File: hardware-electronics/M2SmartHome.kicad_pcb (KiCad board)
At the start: 4 copper layers, 22 x 76 mm, 207 parts, among them J1 M.2-Key-M-edge-connector, J2 Micro_SD_Card_Det_Hirose_DM3AT, J3 CONMHF1-SMD-T, J4 CONMHF1-SMD-T, U1 RTL8188FTV-VC-CG, U10 24AA04T-I_OT, U2 EMMC16G-MW28-01E10, U3 PI7C9X440SLBFDE, U4 24AA04T-I_OT, U5 CP2102N-A02-GQFN20, U6 24AA04T-I_OT, U7 EFR32MG21B020F1024IM32-B, U8 USB2244-AEZG-06, U9 USB2244-AEZG-06, Y1 ABM8-12.000MHZ-B2-T, Y2 ECS-240-10-47-CKM-TR, Y3 ECS-240-10-47-CKM-TR, Y5 ABM8-40.000MHZ-B2-T

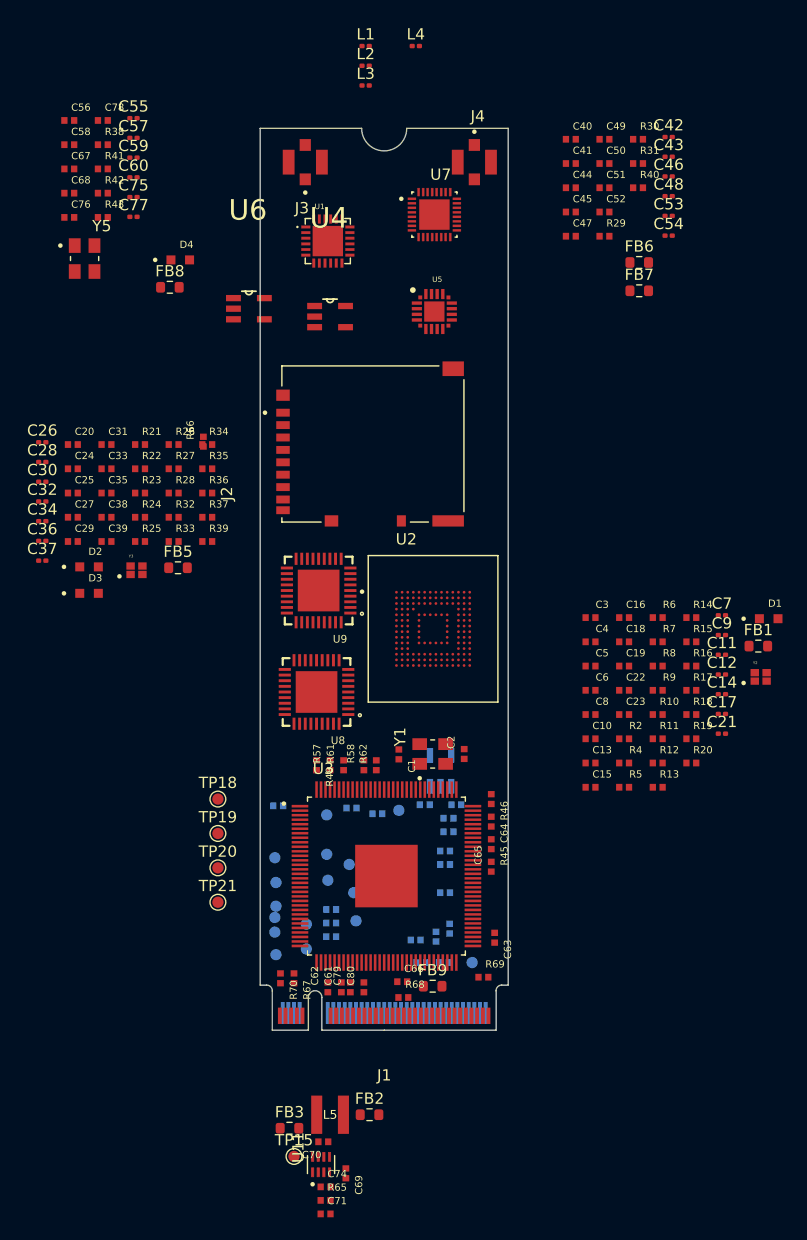
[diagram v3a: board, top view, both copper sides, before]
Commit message: [#13] WIP Placement wifi
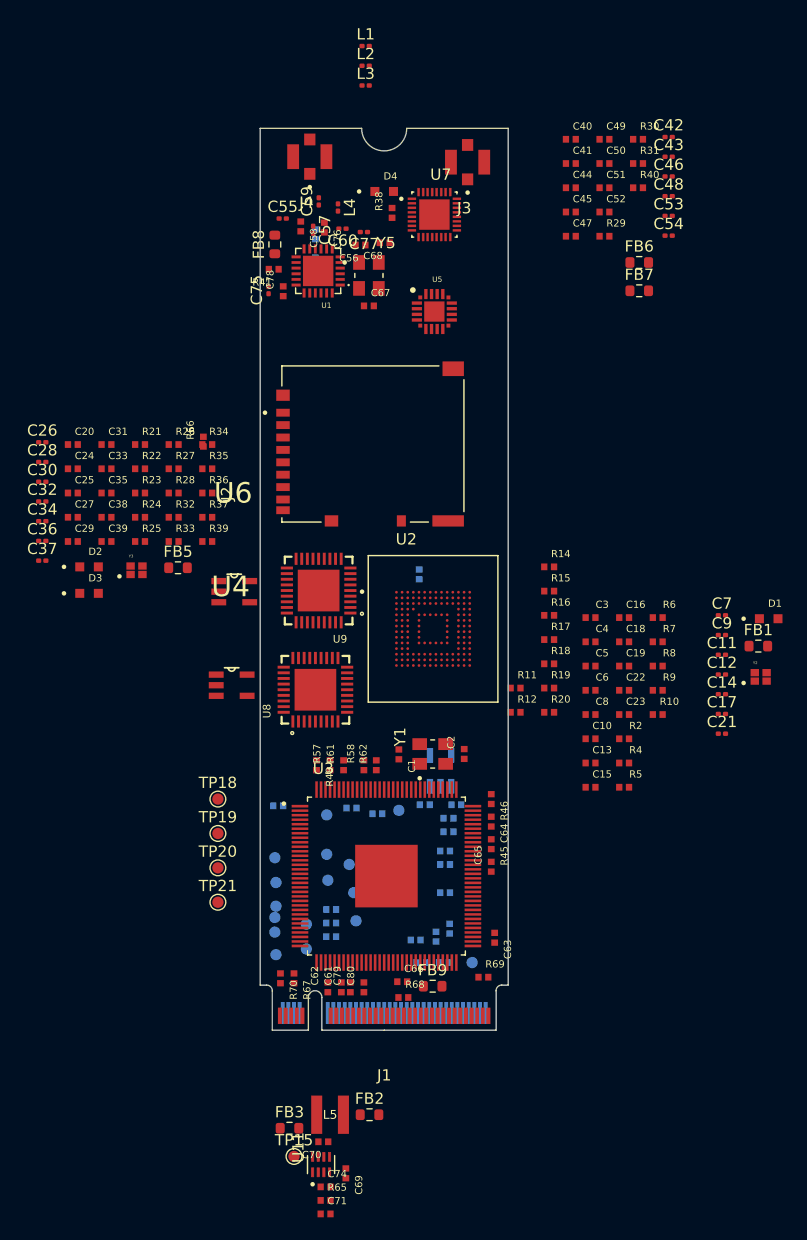
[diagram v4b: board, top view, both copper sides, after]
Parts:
- R13, R42, R43: moved to B.Cu
- moved U4 33.8 mm to (78.5, 135.4)
- moved C67 29.2 mm to (90.6, 101.8)
- moved R13 28.4 mm to (95.1, 125.6), turned to 90 degrees
- moved C68 28.3 mm to (92.0, 96.2), turned to 180 degrees
- moved C56 28.1 mm to (89.9, 96.3), turned to 180 degrees
- moved R38 26.4 mm to (92.7, 93.5), turned to 90 degrees
- moved Y5 25.3 mm to (90.6, 99.0)
- moved U6 25.1 mm to (78.7, 127.1)
- moved C76 22.7 mm to (86.7, 94.8), turned to -90 degrees
- moved C78 22.0 mm to (83.0, 100.5), turned to 90 degrees
- moved C58 21.8 mm to (84.6, 94.7), turned to -90 degrees
- moved C77 20.5 mm to (90.2, 95.2), turned to 180 degrees
- moved R43 19.3 mm to (85.9, 97.9), turned to 90 degrees
- moved R42 19.2 mm to (85.9, 95.4), turned to 90 degrees
- moved C60 19.1 mm to (88.3, 94.9), turned to 180 degrees
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
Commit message: [#13] WIP Placement wifi
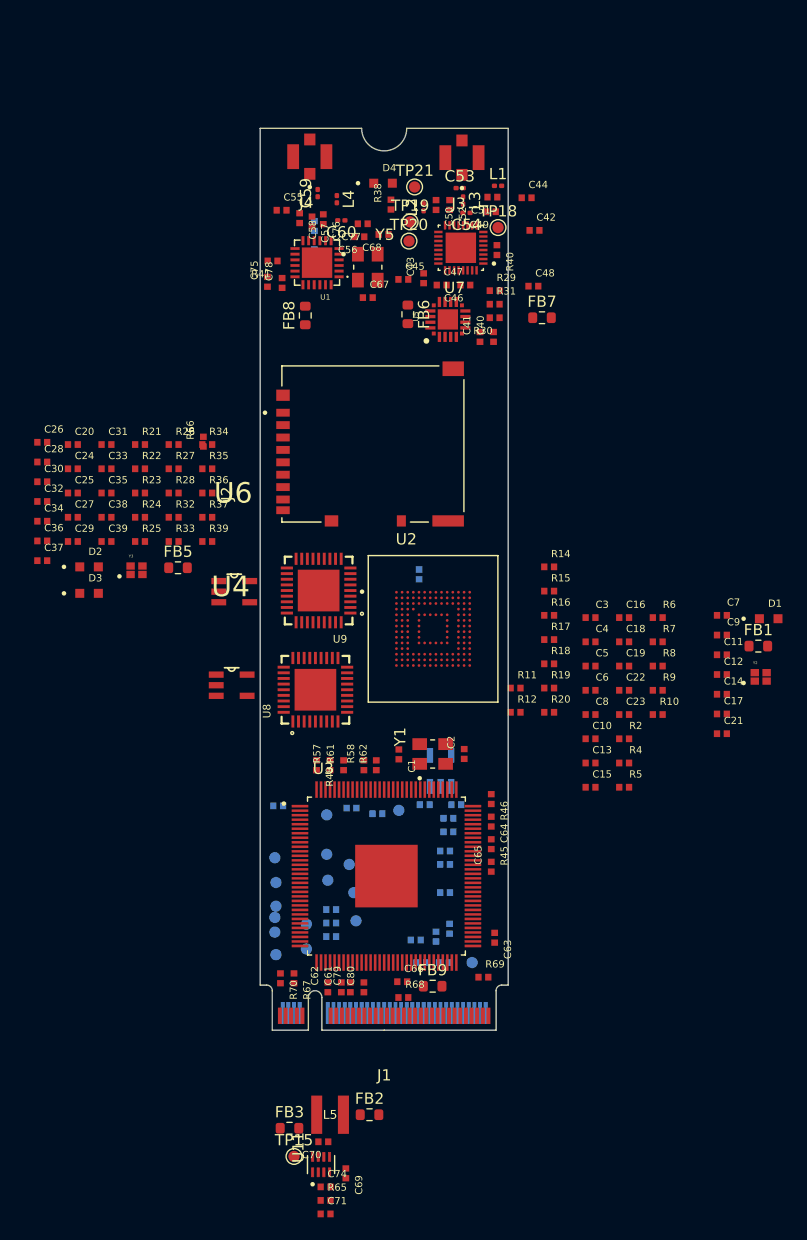
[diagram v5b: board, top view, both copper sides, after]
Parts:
- C11, C12, C14, C17, C21, C26, C28, C30, C32, C34, C36, C37, C42, C43, C46, C48, C55, C57, C7, C75, C77, C9: footprint M2SmartHomeFootprints:C_0201 -> M2SmartHomeFootprints:C_0402
- moved TP21 65.8 mm to (94.7, 91.2)
- moved TP20 58.1 mm to (94.2, 96.0)
- moved TP19 56.9 mm to (94.3, 94.3)
- moved TP18 56.5 mm to (102.1, 94.8)
- moved C43 24.3 mm to (95.5, 99.3), turned to 90 degrees
- moved FB6 21.0 mm to (94.1, 102.5), turned to -90 degrees
- moved C46 20.4 mm to (99.2, 99.9), turned to 180 degrees
- moved R30 20.3 mm to (101.8, 102.8), turned to 180 degrees
- moved C40 18.8 mm to (101.7, 104.5), turned to 90 degrees
- moved C53 18.7 mm to (98.7, 91.3)
- moved C54 18.0 mm to (99.3, 93.5), turned to 180 degrees
- moved R31 17.8 mm to (101.8, 101.6)
- moved C41 17.4 mm to (100.5, 104.5), turned to 90 degrees
- moved L1 17.1 mm to (102.1, 91.1)
- moved C45 16.0 mm to (93.7, 99.4)
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
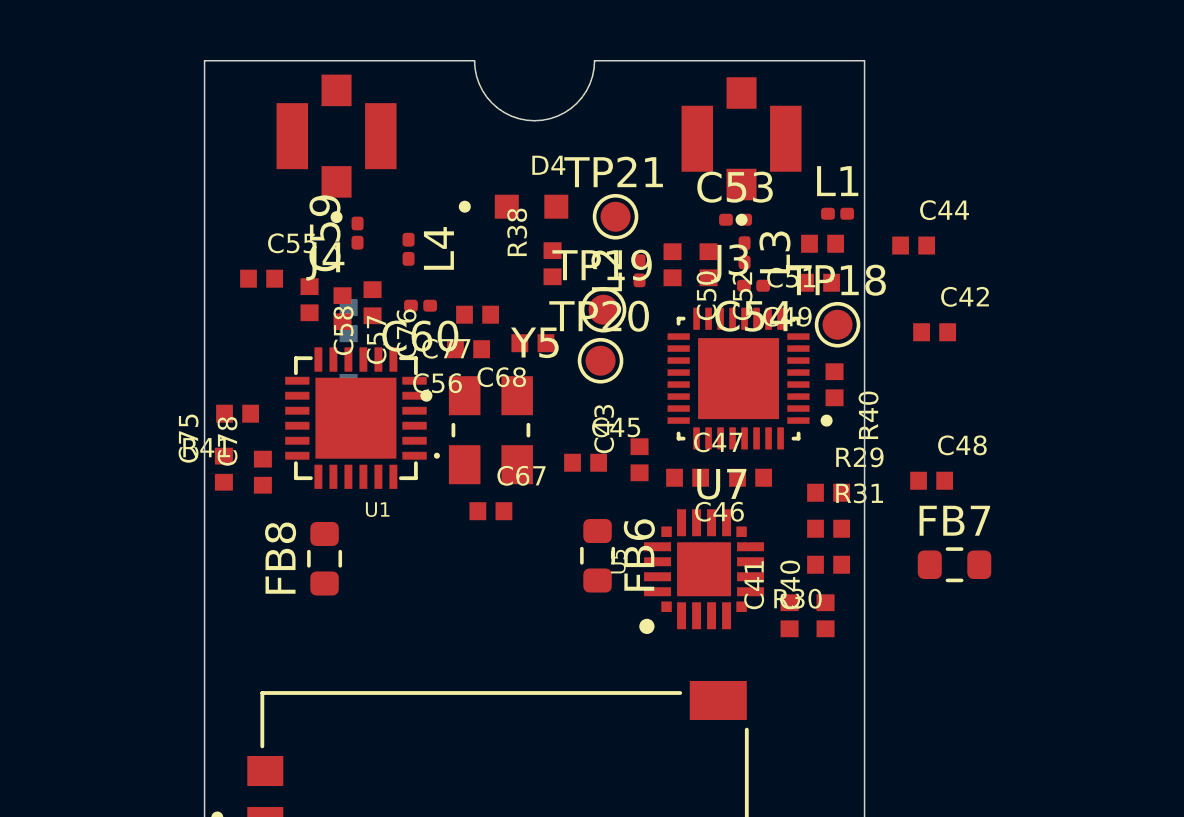
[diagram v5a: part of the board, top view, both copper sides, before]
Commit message: [#13] WIP Placement wifi
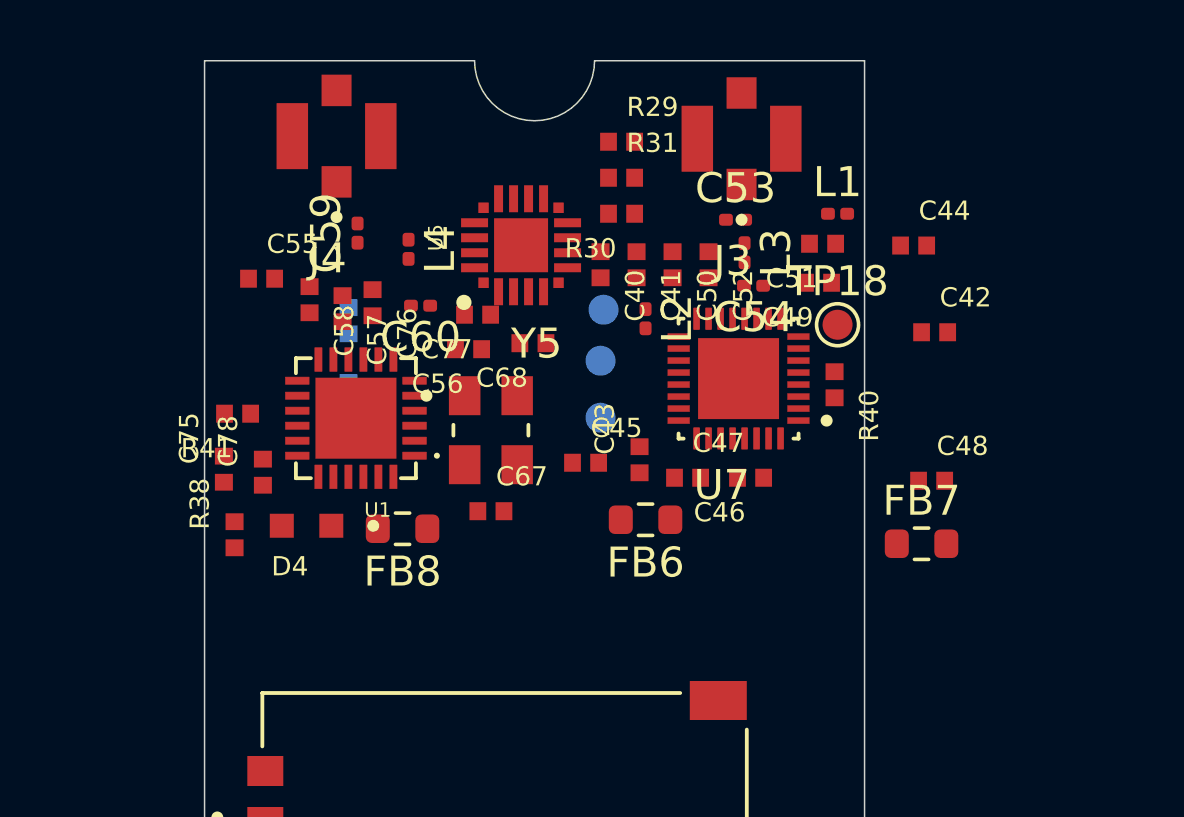
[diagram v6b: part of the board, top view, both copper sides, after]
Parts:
- TP19, TP20, TP21: moved to B.Cu
- moved R38 13.9 mm to (82.0, 101.8)
- moved C40 13.9 mm to (94.2, 92.8), turned to -90 degrees
- moved R29 13.6 mm to (94.9, 88.7)
- moved R30 13.6 mm to (94.9, 91.1)
- moved R31 13.6 mm to (94.9, 89.9)
- moved D4 13.0 mm to (84.4, 101.5), turned to 180 degrees
- moved C41 12.8 mm to (95.4, 92.8), turned to -90 degrees
- moved U5 12.4 mm to (91.5, 92.2)
- moved TP21 6.72 mm to (94.2, 97.9), turned to 180 degrees
- moved FB8 2.79 mm to (87.6, 101.6), turned to 180 degrees
- moved FB6 2.00 mm to (95.7, 101.3), turned to 180 degrees
- moved L2 1.61 mm to (95.7, 94.6), turned to -90 degrees
- moved FB7 1.30 mm to (104.9, 102.1)
- turned TP19 to 180 degrees
- turned TP20 to 180 degrees

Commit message: [#13] WIP Placement eMMC
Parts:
- C15, C16, C17, C18, C19, C21, C22, C23: moved to B.Cu
- moved C17 42.0 mm to (80.0, 139.0), turned to 180 degrees
- moved C12 39.7 mm to (82.9, 127.6)
- moved Y2 39.5 mm to (86.1, 138.1), turned to -90 degrees
- moved C16 35.0 mm to (80.0, 140.3), turned to 180 degrees
- moved R6 34.6 mm to (82.3, 136.2)
- moved C21 31.9 mm to (92.1, 128.5), turned to 90 degrees
- moved R5 31.3 mm to (82.6, 138.1), turned to 180 degrees
- moved R2 31.1 mm to (84.8, 127.6)
- moved R8 30.3 mm to (86.1, 136.1)
- moved C10 25.9 mm to (84.5, 137.9), turned to 90 degrees
- moved C4 23.6 mm to (87.6, 138.0), turned to -90 degrees
- moved C15 21.3 mm to (94.5, 130.1), turned to 90 degrees
- moved C22 21.2 mm to (93.4, 128.5), turned to 90 degrees
- moved C23 19.3 mm to (95.7, 130.1), turned to 90 degrees
- moved C18 16.4 mm to (96.9, 130.7), turned to -90 degrees
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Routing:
- net Net-(U2-DAT0): track 0.00 -> 0.77 mm

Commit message: [#13] WIP Placement eMMC
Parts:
- C11, C14, C7, C8, C9: moved to B.Cu
- C16: moved to F.Cu
- moved FB1 39.1 mm to (87.0, 140.4), turned to 180 degrees
- moved C11 37.3 mm to (84.7, 132.3), turned to 180 degrees
- moved D1 35.8 mm to (91.4, 138.3)
- moved C7 35.7 mm to (86.3, 129.8), turned to 90 degrees
- moved C9 35.3 mm to (86.8, 133.7), turned to -90 degrees
- moved C14 34.1 mm to (88.0, 133.6), turned to -90 degrees
- moved C5 29.3 mm to (83.2, 144.8), turned to 180 degrees
- moved C13 28.7 mm to (85.9, 127.2), turned to -90 degrees
- moved C3 23.0 mm to (88.3, 136.1), turned to 180 degrees
- moved R9 22.5 mm to (93.9, 138.3), turned to 180 degrees
- moved C8 21.0 mm to (90.4, 131.4), turned to 180 degrees
- moved C17 9.24 mm to (84.7, 131.1)
- moved C16 8.43 mm to (81.6, 132.0), turned to 90 degrees
- moved R2 1.68 mm to (83.2, 127.2), turned to -90 degrees
- moved C12 0.95 mm to (82.0, 127.2), turned to 90 degrees
